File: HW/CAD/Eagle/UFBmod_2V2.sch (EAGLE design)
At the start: 210 parts, among them J1411 ABRACON_ARJE-0034, T0551 MMBT2222, U0501 MIDAS_MCCOG21605B6W-FPTLWI, U0601 MAX5217, U0701 AT86RF215-ZU, U0711 ASVTX-13-D-26.000MHZ-I05-T, U0811 PE4259, U0821 RFX1010, U0881 B39871B3440U410, U0911 FT232HL, U1101 TPS53353, U1211 TPS62745DSSR, X0891 ANTENNATINY, X0895 ANTENNATINY, X1011 TTE_EN11-HSM, X1311 MOLEX 105017-0001, X1351 PHOENIX_1990067_1X8X2MM50_PTS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, X1361 PHOENIX_1990067_1X8X2MM50_PTS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

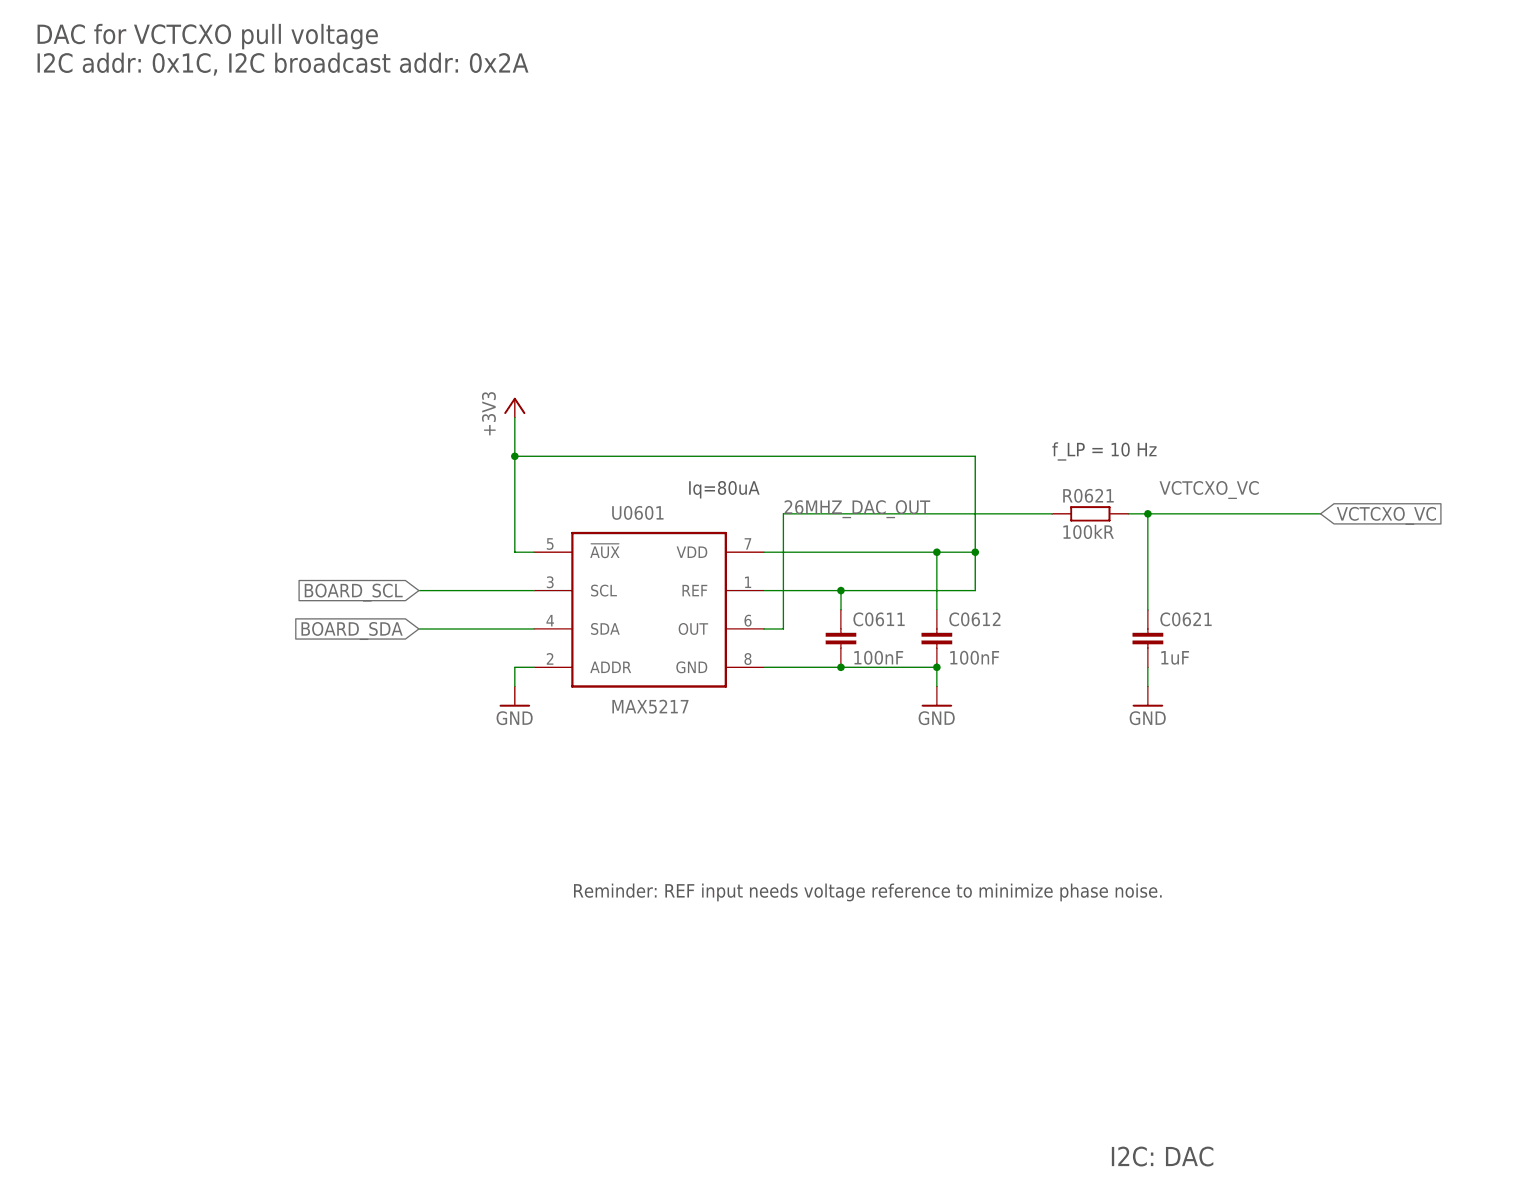
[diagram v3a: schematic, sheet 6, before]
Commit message: HW - Eagle - V2.2 - font size changed for DAC and volt. reference
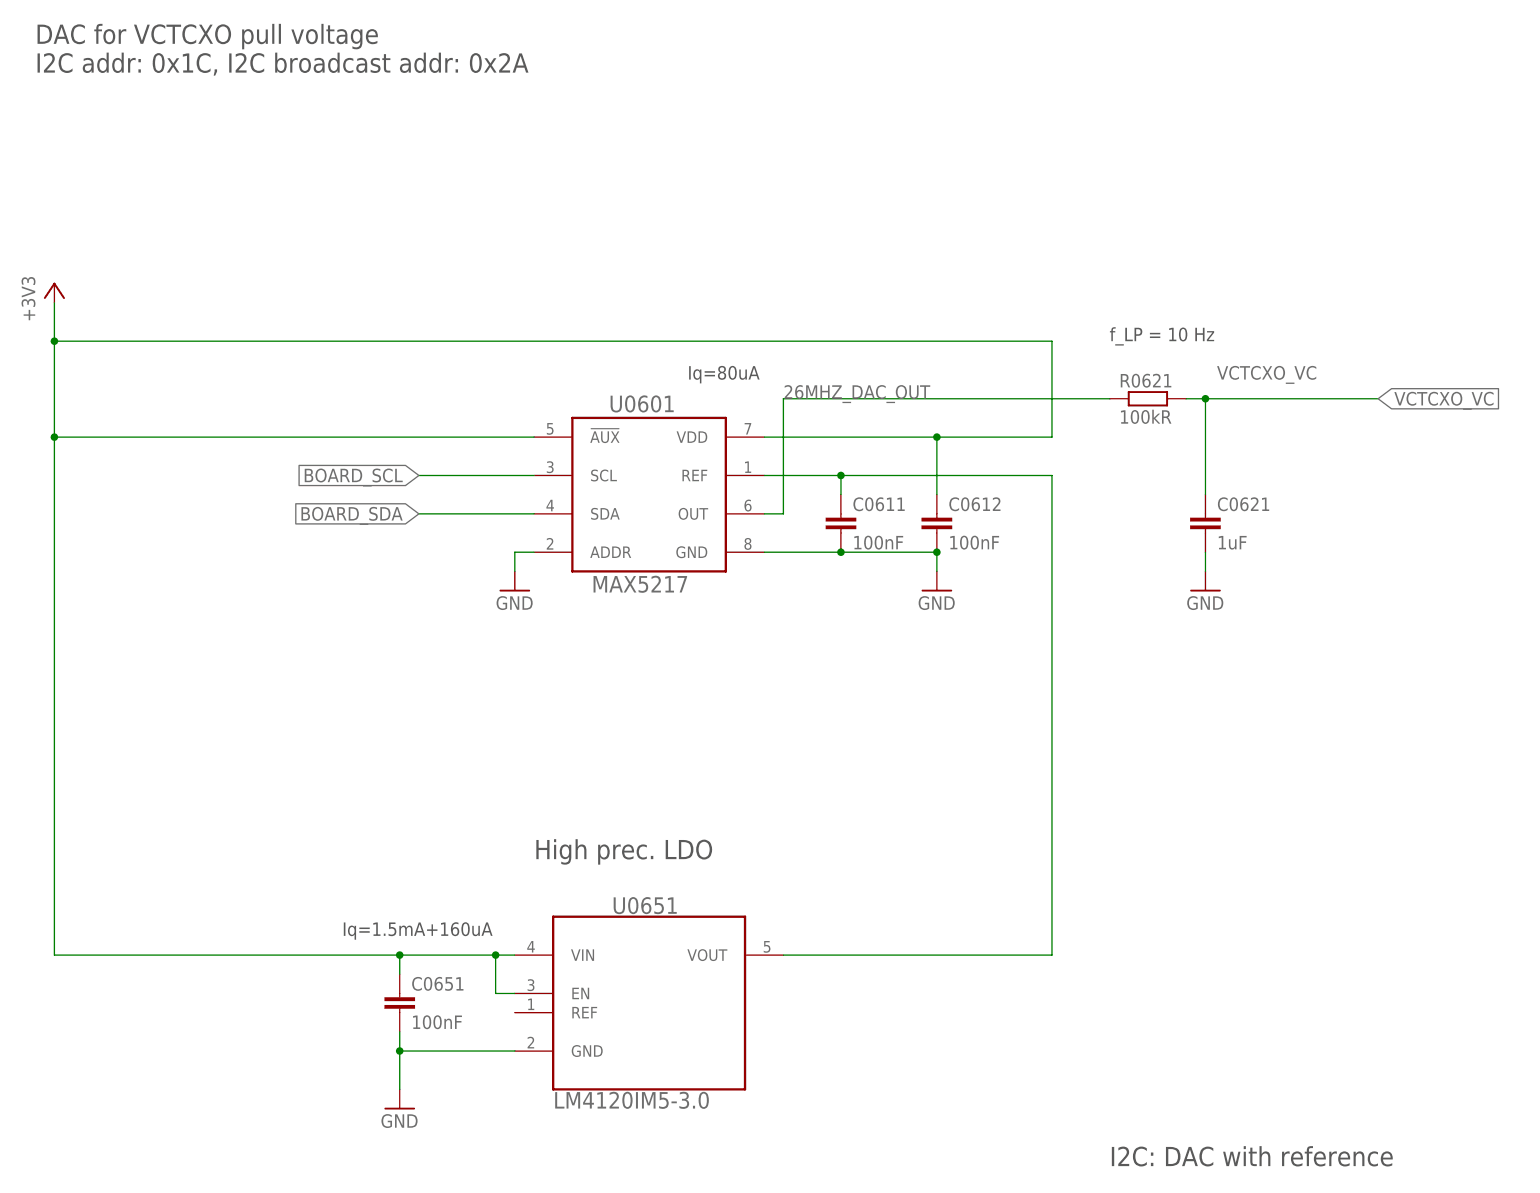
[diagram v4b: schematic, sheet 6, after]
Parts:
- added C0651: 100nF, df4iah_rcl:C-EUC0402
- added U0651: LM4120IM5-3.0, df4iah_powersupply:LM4120IM5-3.0
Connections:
- new net +3V0_20MHZ_VCTCXO: C0611.1, U0601.REF, U0651.VOUT
- net +3V3: now also C0651.1, U0651.EN, U0651.VIN; no longer C0611.1, U0601.REF
- net GND: now also C0651.2, U0651.GND
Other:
- note added: "High prec. LDO"
- note added: "I2C: DAC with reference"
- note added: "Iq=1.5mA+160uA"
- note removed: "I2C: DAC"
- note removed: "Reminder: REF input needs voltage reference to minimize phase noise."
- moved on the sheet: C0611, C0612, C0621, R0621, U0601

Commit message: HW - Eagle - V2.2 - Ethernet magnetics LED resistor values modified (V2.1 also)
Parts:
- R1421, R1422: value 1kR -> 470R
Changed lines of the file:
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@@
 <part name="GND1412" library="df4iah_supply" deviceset="GND" device=""/>
 <part name="GND1413" library="df4iah_supply" deviceset="GND" device=""/>
-<part name="R1421" library="df4iah_rcl" deviceset="R-EU_" device="R0402" value="1kR"/>
-<part name="R1422" library="df4iah_rcl" deviceset="R-EU_" device="R0402" value="1kR"/>
+<part name="R1421" library="df4iah_rcl" deviceset="R-EU_" device="R0402" value="470R"/>
+<part name="R1422" library="df4iah_rcl" deviceset="R-EU_" device="R0402" value="470R"/>
 <part name="+3V3_1431" library="df4iah_supply" deviceset="+3V3" device=""/>
 <part name="+3V3_1441" library="df4iah_supply" deviceset="+3V3" device=""/>

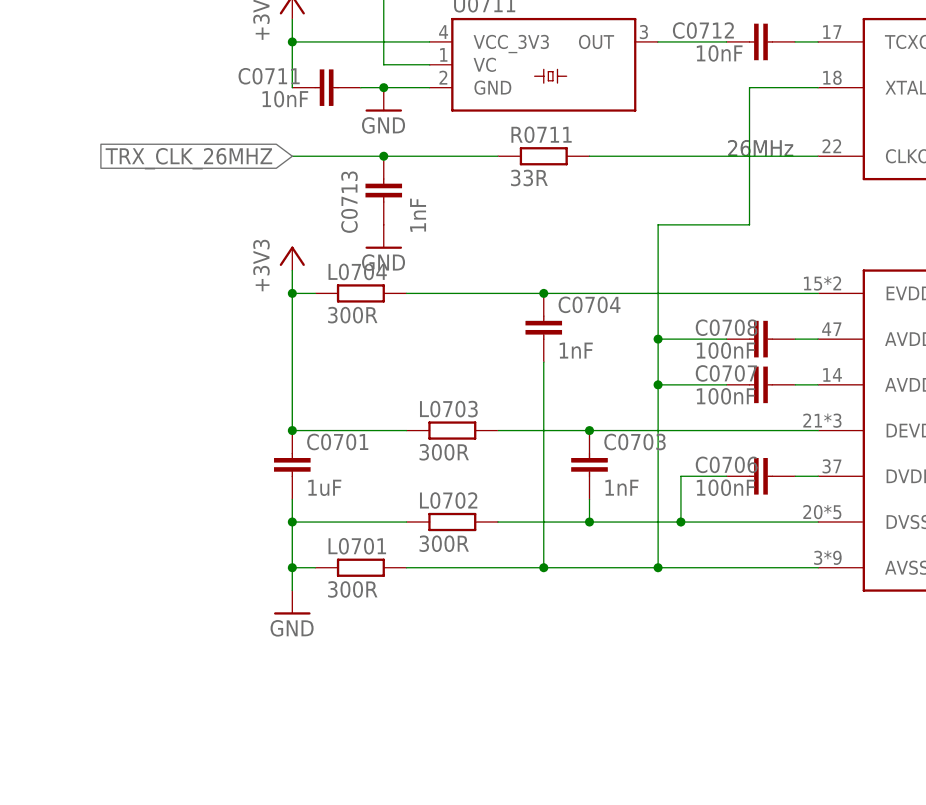
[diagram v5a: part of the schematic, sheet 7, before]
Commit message: HW - Eagle - V2.1 V2.2 - TRX corrections added
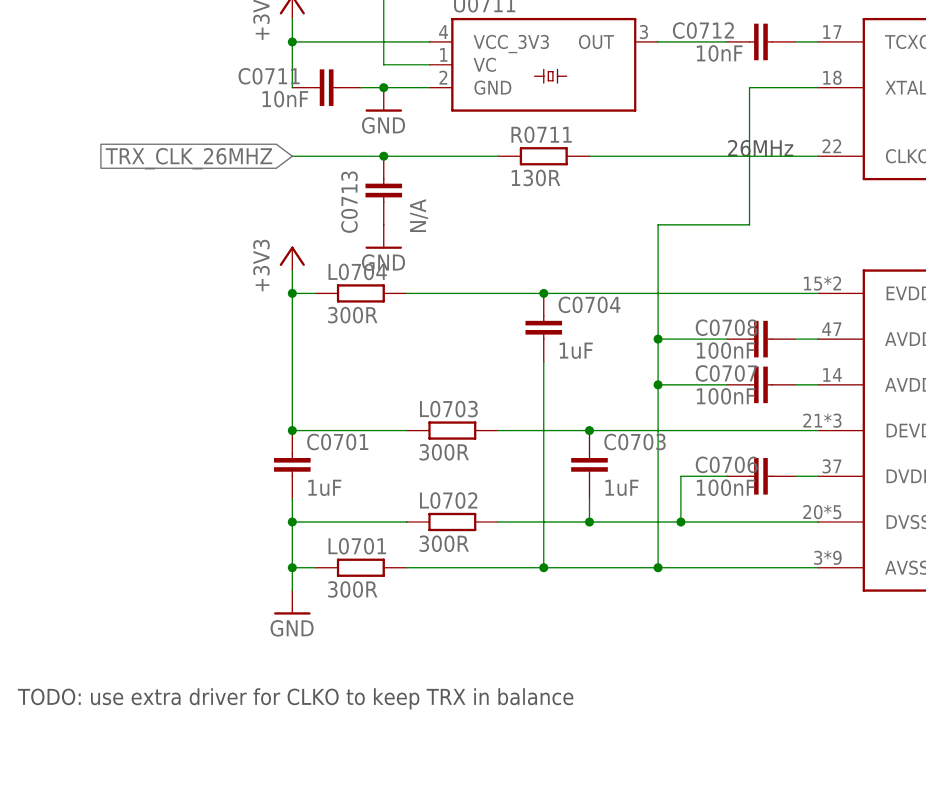
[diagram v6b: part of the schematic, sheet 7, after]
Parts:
- C0703, C0704: value 1nF -> 1uF
- C0713: value 1nF -> N/A
- R0711: value 33R -> 130R
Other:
- note added: "TODO: use extra driver for CLKO to keep TRX in balance"
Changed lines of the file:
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@@
 <part name="L0704" library="df4iah_rcl" deviceset="R-EU_" device="R1206" value="300R"/>
 <part name="+3V3_0701" library="df4iah_supply" deviceset="+3V3" device=""/>
-<part name="C0704" library="df4iah_rcl" deviceset="C-EU" device="C0402" value="1nF"/>
-<part name="C0703" library="df4iah_rcl" deviceset="C-EU" device="C0402" value="1nF"/>
+<part name="C0704" library="df4iah_rcl" deviceset="C-EU" device="C0402" value="1uF"/>
+<part name="C0703" library="df4iah_rcl" deviceset="C-EU" device="C0402" value="1uF"/>
 <part name="C0706" library="df4iah_rcl" deviceset="C-EU" device="C0402" value="100nF"/>
 <part name="C0708" library="df4iah_rcl" deviceset="C-EU" device="C0402" value="100nF"/>
@@
 <part name="S1321" library="df4iah_switch" deviceset="KSR223G_SMD_1POL" device=""/>
 <part name="R1321" library="df4iah_rcl" deviceset="R-EU_" device="R0402" value="1kR"/>
-<part name="R0711" library="df4iah_rcl" deviceset="R-EU_" device="R0402" value="33R"/>
+<part name="R0711" library="df4iah_rcl" deviceset="R-EU_" device="R0402" value="130R"/>
 <part name="C1321" library="df4iah_rcl" deviceset="C-EU" device="C0402" value="100nF"/>
 <part name="GND0001" library="df4iah_supply" deviceset="GND" device=""/>
-<part name="C0713" library="df4iah_rcl" deviceset="C-EU" device="C0402" value="1nF"/>
+<part name="C0713" library="df4iah_rcl" deviceset="C-EU" device="C0402" value="N/A"/>
 <part name="GND0712" library="df4iah_supply" deviceset="GND" device=""/>
 <part name="FPGA_EN1" library="df4iah_connector" deviceset="TP" device="B1,27"/>
@@
 <text x="22.86" y="162.56" size="2.54" layer="97" ratio="15">Microchip Technologies AT86RF215</text>
 <text x="93.98" y="83.82" size="1.778" layer="97">26MHz</text>
+<text x="15.24" y="22.86" size="1.778" layer="97">TODO: use extra driver for CLKO to keep TRX in balance</text>
 </plain>
 <instances>

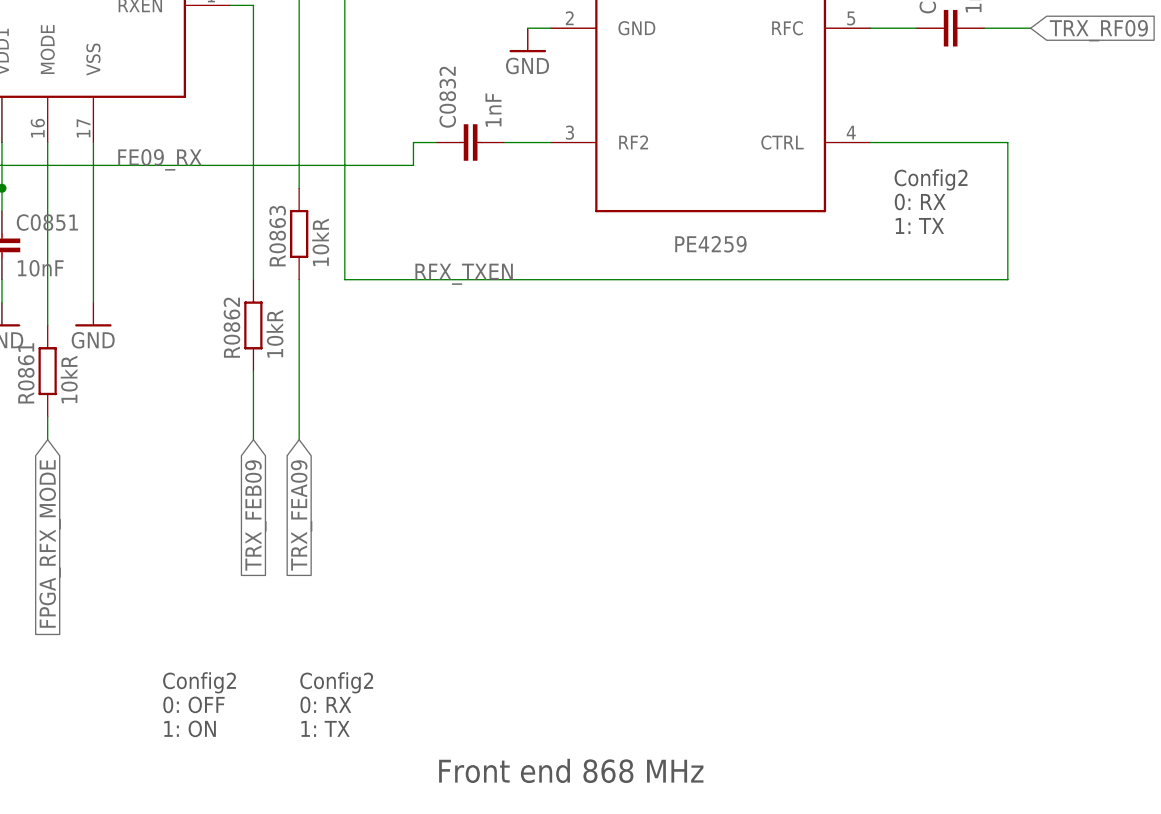
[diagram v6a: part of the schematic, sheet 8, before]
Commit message: HW - Eagle - V2.1 V2.2 - TRX frontend pins configuration 1, not 2
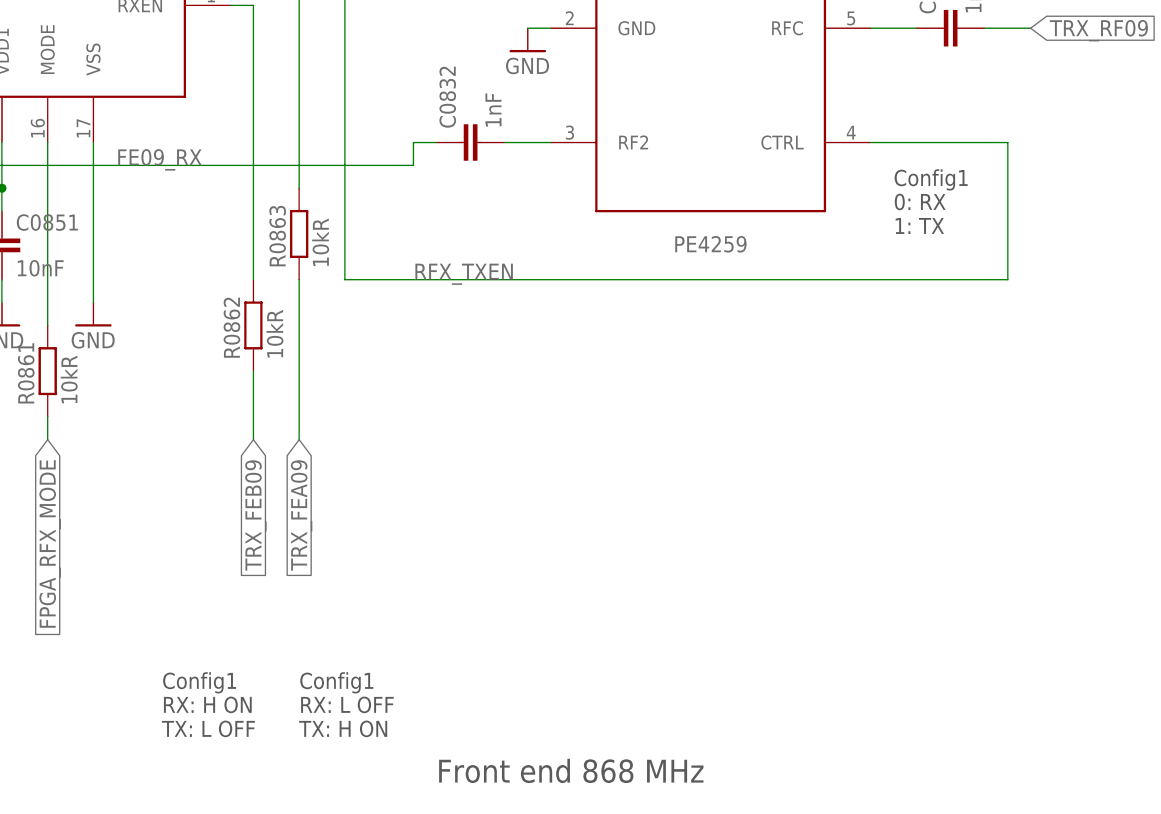
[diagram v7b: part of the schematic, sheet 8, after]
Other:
- note added: "Config1 0: RX 1: TX"
- note added: "Config1 RX: H ON TX: L OFF"
- note added: "Config1 RX: L OFF TX: H ON"
- note removed: "Config2 0: OFF 1: ON"
- note removed: "Config2 0: RX 1: TX"
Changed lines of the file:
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@@
 <text x="22.86" y="162.56" size="2.54" layer="97" ratio="15">Front end: LNA &amp; PA for 868 MHz</text>
 <text x="165.1" y="15.24" size="2.54" layer="97" ratio="15">Front end 868 MHz</text>
-<text x="215.9" y="76.2" size="1.778" layer="97">Config2
+<text x="215.9" y="76.2" size="1.778" layer="97">Config1
 0: RX
 1: TX</text>
-<text x="134.62" y="20.32" size="1.778" layer="97">Config2
-0: OFF
-1: ON</text>
-<text x="149.86" y="20.32" size="1.778" layer="97">Config2
-0: RX
-1: TX</text>
+<text x="134.62" y="20.32" size="1.778" layer="97">Config1
+RX: H ON
+TX: L OFF</text>
+<text x="149.86" y="20.32" size="1.778" layer="97">Config1
+RX: L OFF
+TX: H ON</text>
 <text x="7.62" y="121.92" size="1.778" layer="97">X0891</text>
 <text x="7.62" y="40.64" size="1.778" layer="97">X0895</text>
